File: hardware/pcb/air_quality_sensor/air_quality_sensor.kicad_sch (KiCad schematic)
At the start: 91 parts, among them J1 USB4110, J2 QWIIC Connector, SW1 Push_Button, SW2 Push_Button, U1 TLV62569A, U2 SHT40, U3 BMP280, U4 TPD2EUSB30, U5 SCD41, U6 SGP41, U7 TPS7A20, U8 ESP32-C3-WROOM-02, U9 TLV75533P

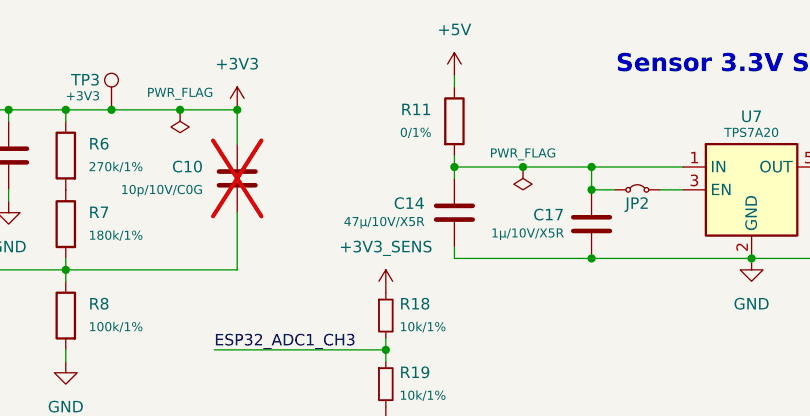
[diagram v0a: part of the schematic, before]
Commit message: Fix LED boot crash, persist brightness, add self-heating offsets
- Guard LED script with 5s boot delay to avoid WS2812 driver crash
- Persist user brightness in dedicated NVS global instead of remote_values
- Drop LED transition fade (instant color updates)
- Add empirical self-heating offsets: SHT40 −5.5 °C/+8 %RH,
  SCD41 −1.5 °C/+4 %RH, BMP280 −5.5 °C
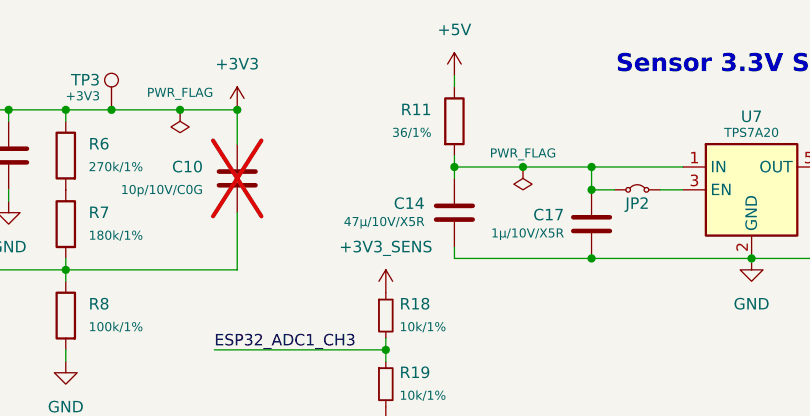
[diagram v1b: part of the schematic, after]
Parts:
- R11: value 0/1% -> 36/1%
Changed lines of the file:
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@@
 			)
 		)
-		(property "Value" "0/1%"
+		(property "Value" "36/1%"
 			(at 133.35 33.02 0)
 			(show_name no)

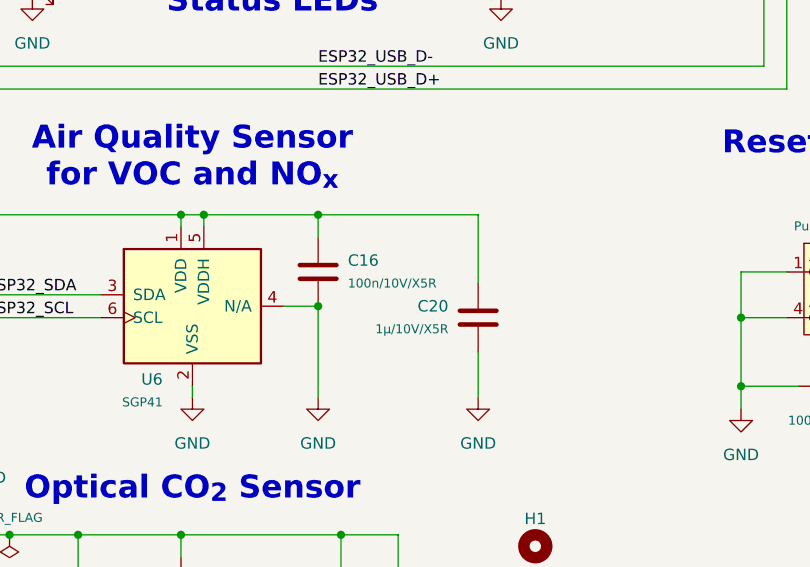
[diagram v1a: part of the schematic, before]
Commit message: changed C16 to 1uF to prevent SGP41 from making weird noises..
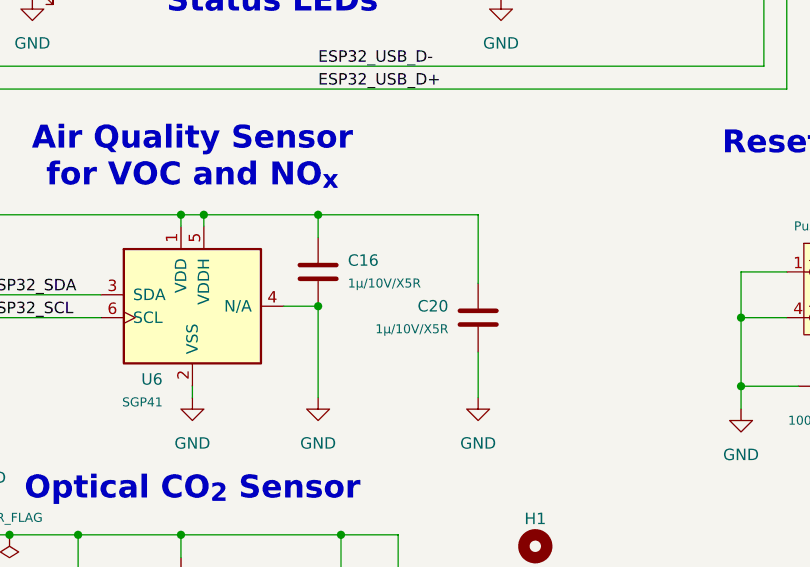
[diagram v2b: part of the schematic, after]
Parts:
- C16: value 100n/10V/X5R -> 1µ/10V/X5R
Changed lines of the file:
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@@
 			)
 		)
-		(property "Value" "100n/10V/X5R"
+		(property "Value" "1µ/10V/X5R"
 			(at 151.892 140.97 0)
 			(show_name no)
